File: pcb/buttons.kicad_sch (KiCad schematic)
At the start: 91 parts, among them J3 MSP_SBW, SW1 Off, SW10 R_LCD3, SW11 R_LCD4, SW12 LCD_LEFT, SW13 LCD_RIGHT, SW14 Glow, SW15 Device, SW16 Media, SW17 Mute, SW18 Prev, SW19 Vol+, SW2 Activities, SW20 Vol-, SW21 Ch+, SW22 Ch-, SW23 Dpad_Up, SW24 Dpad_Left, SW25 Dpad_Right, SW26 Dpad_Down, SW27 Dpad_OK, SW28 PgUp, SW29 PgDown, SW3 Help, SW30 Menu, SW31 Exit, SW32 Guide, SW33 Info, SW34 Stop, SW35 Replay, SW36 Skip, SW37 Play, SW38 Rec, SW39 Rew, SW4 L_LCD1, SW40 Fwd, SW41 Pause, SW42 KP_1, SW43 KP_2, SW44 KP_3, SW45 KP_4, SW46 KP_5, SW47 KP_6, SW48 KP_7, SW49 KP_8, SW5 L_LCD2, SW50 KP_9, SW51 KP_0, SW52 KP_Clear, SW53 KP_Enter, SW6 L_LCD3, SW7 L_LCD4, SW8 R_LCD1, SW9 R_LCD2, U1 MSP430G2553IPW28

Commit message: alpha2 pcb
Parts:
- D1, D10, D11, D12, D13, D14, D15, D16, D17, D18, D19, D2, D20, D21, D22, D23, D24, D25, D26, D27, D28, D29, D3, D30, D31, D32, D4, D5, D6, D7, D8, D9: footprint 880+:C265_reverse_mount_led -> 880+:C265_reverse_mount_led_DRC
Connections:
- net +3V3 renamed +3.3V
- net MSP_P1.1 renamed ESP_TO_MSP
- net MSP_P1.2 renamed MSP_TO_ESP

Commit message: current working kikad
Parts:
- added SW54: SW_RollingBall, Resistor_SMD:R_1210_3225Metric, symbol 880+:SW_RollingBall
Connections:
- net GND: now also SW54.1
- net at U1.26 (XOUT/P2.7): now also SW54.2
- no-connect marks 1 -> 0
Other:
- moved on the sheet: C3, C4
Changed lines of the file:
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@@
   (junction (at 76.2 185.42) (diameter 0) (color 0 0 0 0)
   )
+  (junction (at 205.74 128.27) (diameter 0) (color 0 0 0 0)
+  )
   (junction (at 53.34 185.42) (diameter 0) (color 0 0 0 0)
   )
@@
   (junction (at 46.99 33.02) (diameter 0) (color 0 0 0 0)
   )
+  (junction (at 218.44 120.65) (diameter 0) (color 0 0 0 0)
+  )
   (junction (at 99.06 171.45) (diameter 0) (color 0 0 0 0)
   )
@@
   (junction (at 57.15 55.88) (diameter 0) (color 0 0 0 0)
   )
-  (junction (at 228.6 123.19) (diameter 0) (color 0 0 0 0)
-  )
   (junction (at 53.34 132.08) (diameter 0) (color 0 0 0 0)
   )
@@
   (junction (at 57.15 30.48) (diameter 0) (color 0 0 0 0)
   )
+  (junction (at 195.58 119.38) (diameter 0) (color 0 0 0 0)
+  )
   (junction (at 46.99 45.72) (diameter 0) (color 0 0 0 0)
   )
@@
   (junction (at 80.01 71.12) (diameter 0) (color 0 0 0 0)
   )
-  (junction (at 238.76 114.3) (diameter 0) (color 0 0 0 0)
-  )
   (junction (at 68.58 146.05) (diameter 0) (color 0 0 0 0)
   )
@@
   (junction (at 45.72 132.08) (diameter 0) (color 0 0 0 0)
   )
+  (junction (at 218.44 128.27) (diameter 0) (color 0 0 0 0)
+  )
   (junction (at 45.72 146.05) (diameter 0) (color 0 0 0 0)
   )
@@
   (junction (at 80.01 58.42) (diameter 0) (color 0 0 0 0)
   )
+  (junction (at 218.44 111.76) (diameter 0) (color 0 0 0 0)
+  )
   (junction (at 90.17 43.18) (diameter 0) (color 0 0 0 0)
   )
@@
   (junction (at 40.64 55.88) (diameter 0) (color 0 0 0 0)
   )
-  (junction (at 218.44 123.19) (diameter 0) (color 0 0 0 0)
-  )
   (junction (at 83.82 173.99) (diameter 0) (color 0 0 0 0)
   )
@@
   (junction (at 46.99 96.52) (diameter 0) (color 0 0 0 0)
   )
-  (no_connect (at 254 105.41))
   (wire (pts (xy 254 81.28) (xy 256.54 81.28))
     (stroke (width 0) (type default))
@@
     (stroke (width 0) (type default))
   )
+  (wire (pts (xy 218.44 120.65) (xy 241.3 120.65))
+    (stroke (width 0) (type default))
+  )
   (wire (pts (xy 45.72 157.48) (xy 45.72 154.94))
     (stroke (width 0) (type default))
@@
     (stroke (width 0) (type default))
   )
-  (wire (pts (xy 218.44 123.19) (xy 218.44 124.46))
+  (wire (pts (xy 218.44 128.27) (xy 218.44 130.81))
     (stroke (width 0) (type default))
   )
@@
     (stroke (width 0) (type default))
   )
-  (wire (pts (xy 228.6 123.19) (xy 238.76 123.19))
+  (wire (pts (xy 195.58 128.27) (xy 205.74 128.27))
     (stroke (width 0) (type default))
   )
@@
     (stroke (width 0) (type default))
   )
-  (wire (pts (xy 218.44 111.76) (xy 218.44 123.19))
+  (wire (pts (xy 218.44 110.49) (xy 218.44 111.76))
     (stroke (width 0) (type default))
   )
@@
     (stroke (width 0) (type default))
   )
-  (wire (pts (xy 261.62 113.03) (xy 261.62 114.3))
-    (stroke (width 0) (type default))
-  )
   (wire (pts (xy 83.82 146.05) (xy 83.82 147.32))
     (stroke (width 0) (type default))
@@
     (stroke (width 0) (type default))
   )
+  (wire (pts (xy 218.44 120.65) (xy 218.44 128.27))
+    (stroke (width 0) (type default))
+  )
   (wire (pts (xy 53.34 160.02) (xy 53.34 161.29))
     (stroke (width 0) (type default))
@@
     (stroke (width 0) (type default))
   )
+  (wire (pts (xy 254 105.41) (xy 260.35 105.41))
+    (stroke (width 0) (type default))
+  )
   (wire (pts (xy 80.01 45.72) (xy 96.52 45.72))
     (stroke (width 0) (type default))
@@
     (stroke (width 0) (type default))
   )
-  (wire (pts (xy 218.44 123.19) (xy 228.6 123.19))
+  (wire (pts (xy 205.74 128.27) (xy 218.44 128.27))
     (stroke (width 0) (type default))
   )
@@
     (stroke (width 0) (type default))
   )
-  (wire (pts (xy 228.6 123.19) (xy 228.6 121.92))
+  (wire (pts (xy 195.58 128.27) (xy 195.58 127))
     (stroke (width 0) (type default))
   )
@@
     (stroke (width 0) (type default))
   )
-  (wire (pts (xy 238.76 123.19) (xy 238.76 121.92))
+  (wire (pts (xy 205.74 128.27) (xy 205.74 127))
     (stroke (width 0) (type default))
   )
@@
     (stroke (width 0) (type default))
   )
+  (wire (pts (xy 260.35 105.41) (xy 260.35 120.65))
+    (stroke (width 0) (type default))
+  )
   (wire (pts (xy 90.17 68.58) (xy 90.17 55.88))
     (stroke (width 0) (type default))
@@
     (stroke (width 0) (type default))
   )
+  (wire (pts (xy 260.35 120.65) (xy 251.46 120.65))
+    (stroke (width 0) (type default))
+  )
   (wire (pts (xy 60.96 157.48) (xy 68.58 157.48))
     (stroke (width 0) (type default))
@@
     (stroke (width 0) (type default))
   )
-  (wire (pts (xy 261.62 114.3) (xy 238.76 114.3))
-    (stroke (width 0) (type default))
-  )
   (wire (pts (xy 63.5 96.52) (xy 80.01 96.52))
     (stroke (width 0) (type default))
@@
     (stroke (width 0) (type default))
   )
-  (wire (pts (xy 228.6 114.3) (xy 238.76 114.3))
+  (wire (pts (xy 195.58 119.38) (xy 205.74 119.38))
+    (stroke (width 0) (type default))
+  )
+  (wire (pts (xy 218.44 111.76) (xy 218.44 120.65))
     (stroke (width 0) (type default))
   )
@@
     )
   )
-  (symbol (lib_id "power:GND") (at 218.44 124.46 0) (unit 1)
+  (symbol (lib_id "power:GND") (at 218.44 130.81 0) (unit 1)
     (in_bom yes) (on_board yes) (dnp no) (fields_autoplaced)
-    (property "Reference" "#PWR06" (at 218.44 130.81 0)
+    (property "Reference" "#PWR06" (at 218.44 137.16 0)
       (effects (font (size 1.27 1.27)) hide)
     )
-    (property "Value" "GND" (at 218.44 129.0225 0)
+    (property "Value" "GND" (at 218.44 135.3725 0)
       (effects (font (size 1.27 1.27)))
     )
-    (property "Footprint" "" (at 218.44 124.46 0)
+    (property "Footprint" "" (at 218.44 130.81 0)
       (effects (font (size 1.27 1.27)) hide)
     )
-    (property "Datasheet" "" (at 218.44 124.46 0)
+    (property "Datasheet" "" (at 218.44 130.81 0)
       (effects (font (size 1.27 1.27)) hide)
     )
@@
     )
   )
+  (symbol (lib_id "880+:SW_RollingBall") (at 246.38 120.65 0) (unit 1)
+    (in_bom yes) (on_board yes) (dnp no) (fields_autoplaced)
+    (property "Reference" "SW54" (at 246.38 115.57 0)
+      (effects (font (size 1.27 1.27)))
+    )
+    (property "Value" "SW_RollingBall" (at 246.38 118.11 0)
+      (effects (font (size 1.27 1.27)))
+    )
+    (property "Footprint" "Resistor_SMD:R_1210_3225Metric" (at 246.38 120.65 0)
+      (effects (font (size 1.27 1.27)) hide)
+    )
+    (property "Datasheet" "~" (at 246.38 120.65 0)
+      (effects (font (size 1.27 1.27)) hide)
+    )
+    (pin "1")
+    (pin "2")
+    (instances
+      (project "800+"
+        (path "/e63e39d7-6ac0-4ffd-8aa3-1841a4541b55/ceed2ac1-ff2d-4a48-84e5-5f8d5045fc04"
+          (reference "SW54") (unit 1)
+        )
+      )
+    )
+  )
   (symbol (lib_id "Device:LED") (at 45.72 179.07 90) (unit 1)
     (in_bom yes) (on_board yes) (dnp no) (fields_autoplaced)
@@
     )
   )
-  (symbol (lib_id "power:+3.3V") (at 261.62 113.03 0) (unit 1)
+  (symbol (lib_id "power:+3.3V") (at 195.58 119.38 0) (unit 1)
     (in_bom yes) (on_board yes) (dnp no)
-    (property "Reference" "#PWR019" (at 261.62 116.84 0)
+    (property "Reference" "#PWR019" (at 195.58 123.19 0)
       (effects (font (size 1.27 1.27)) hide)
     )
-    (property "Value" "+3.3V" (at 261.62 109.22 0)
+    (property "Value" "+3.3V" (at 195.58 115.57 0)
       (effects (font (size 1.27 1.27)))
     )
-    (property "Footprint" "" (at 261.62 113.03 0)
+    (property "Footprint" "" (at 195.58 119.38 0)
       (effects (font (size 1.27 1.27)) hide)
     )
-    (property "Datasheet" "" (at 261.62 113.03 0)
+    (property "Datasheet" "" (at 195.58 119.38 0)
       (effects (font (size 1.27 1.27)) hide)
     )
@@
     )
   )
-  (symbol (lib_id "Device:C") (at 228.6 118.11 0) (unit 1)
+  (symbol (lib_id "Device:C") (at 195.58 123.19 0) (unit 1)
     (in_bom yes) (on_board yes) (dnp no) (fields_autoplaced)
-    (property "Reference" "C3" (at 231.521 117.2015 0)
+    (property "Reference" "C3" (at 198.501 122.2815 0)
       (effects (font (size 1.27 1.27)) (justify left))
     )
-    (property "Value" "10u" (at 231.521 119.9766 0)
+    (property "Value" "10u" (at 198.501 125.0566 0)
       (effects (font (size 1.27 1.27)) (justify left))
     )
-    (property "Footprint" "Capacitor_SMD:C_0805_2012Metric" (at 229.5652 121.92 0)
+    (property "Footprint" "Capacitor_SMD:C_0805_2012Metric" (at 196.5452 127 0)
       (effects (font (size 1.27 1.27)) hide)
     )
-    (property "Datasheet" "~" (at 228.6 118.11 0)
+    (property "Datasheet" "~" (at 195.58 123.19 0)
       (effects (font (size 1.27 1.27)) hide)
     )
@@
     )
   )
-  (symbol (lib_id "Device:C") (at 238.76 118.11 0) (unit 1)
+  (symbol (lib_id "Device:C") (at 205.74 123.19 0) (unit 1)
     (in_bom yes) (on_board yes) (dnp no) (fields_autoplaced)
-    (property "Reference" "C4" (at 241.681 117.2015 0)
+    (property "Reference" "C4" (at 208.661 122.2815 0)
       (effects (font (size 1.27 1.27)) (justify left))
     )
-    (property "Value" ".1u" (at 241.681 119.9766 0)
+    (property "Value" ".1u" (at 208.661 125.0566 0)
       (effects (font (size 1.27 1.27)) (justify left))
     )
-    (property "Footprint" "Capacitor_SMD:C_0805_2012Metric" (at 239.7252 121.92 0)
+    (property "Footprint" "Capacitor_SMD:C_0805_2012Metric" (at 206.7052 127 0)
       (effects (font (size 1.27 1.27)) hide)
     )
-    (property "Datasheet" "~" (at 238.76 118.11 0)
+    (property "Datasheet" "~" (at 205.74 123.19 0)
       (effects (font (size 1.27 1.27)) hide)
     )

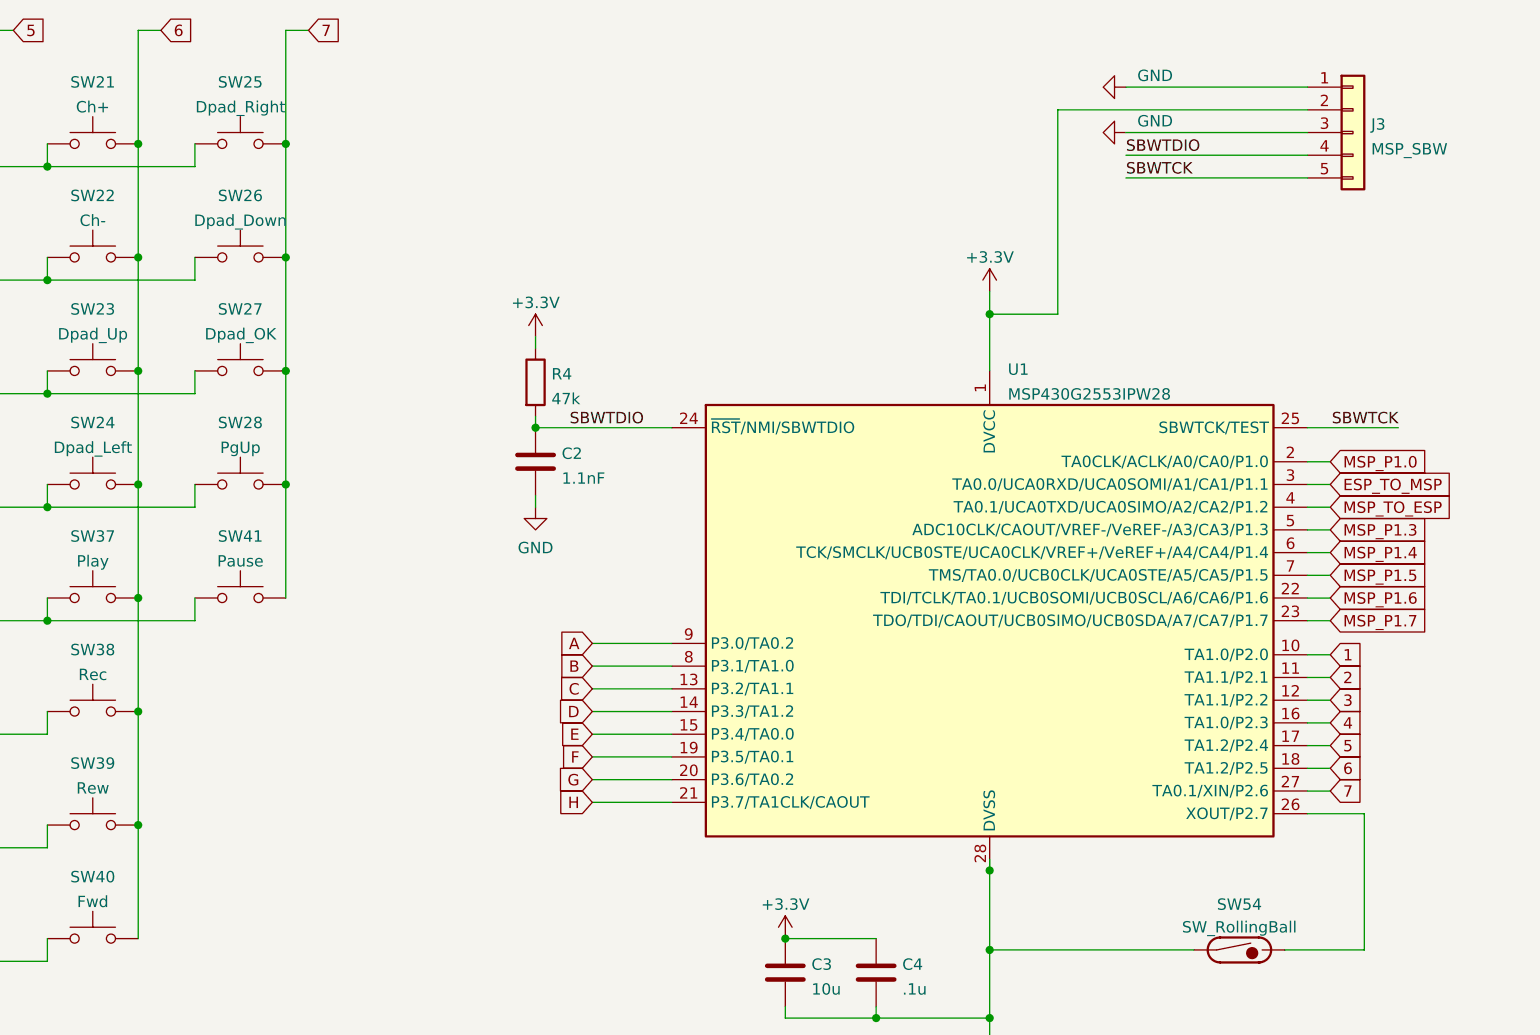
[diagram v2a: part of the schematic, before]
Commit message: add power to schematic
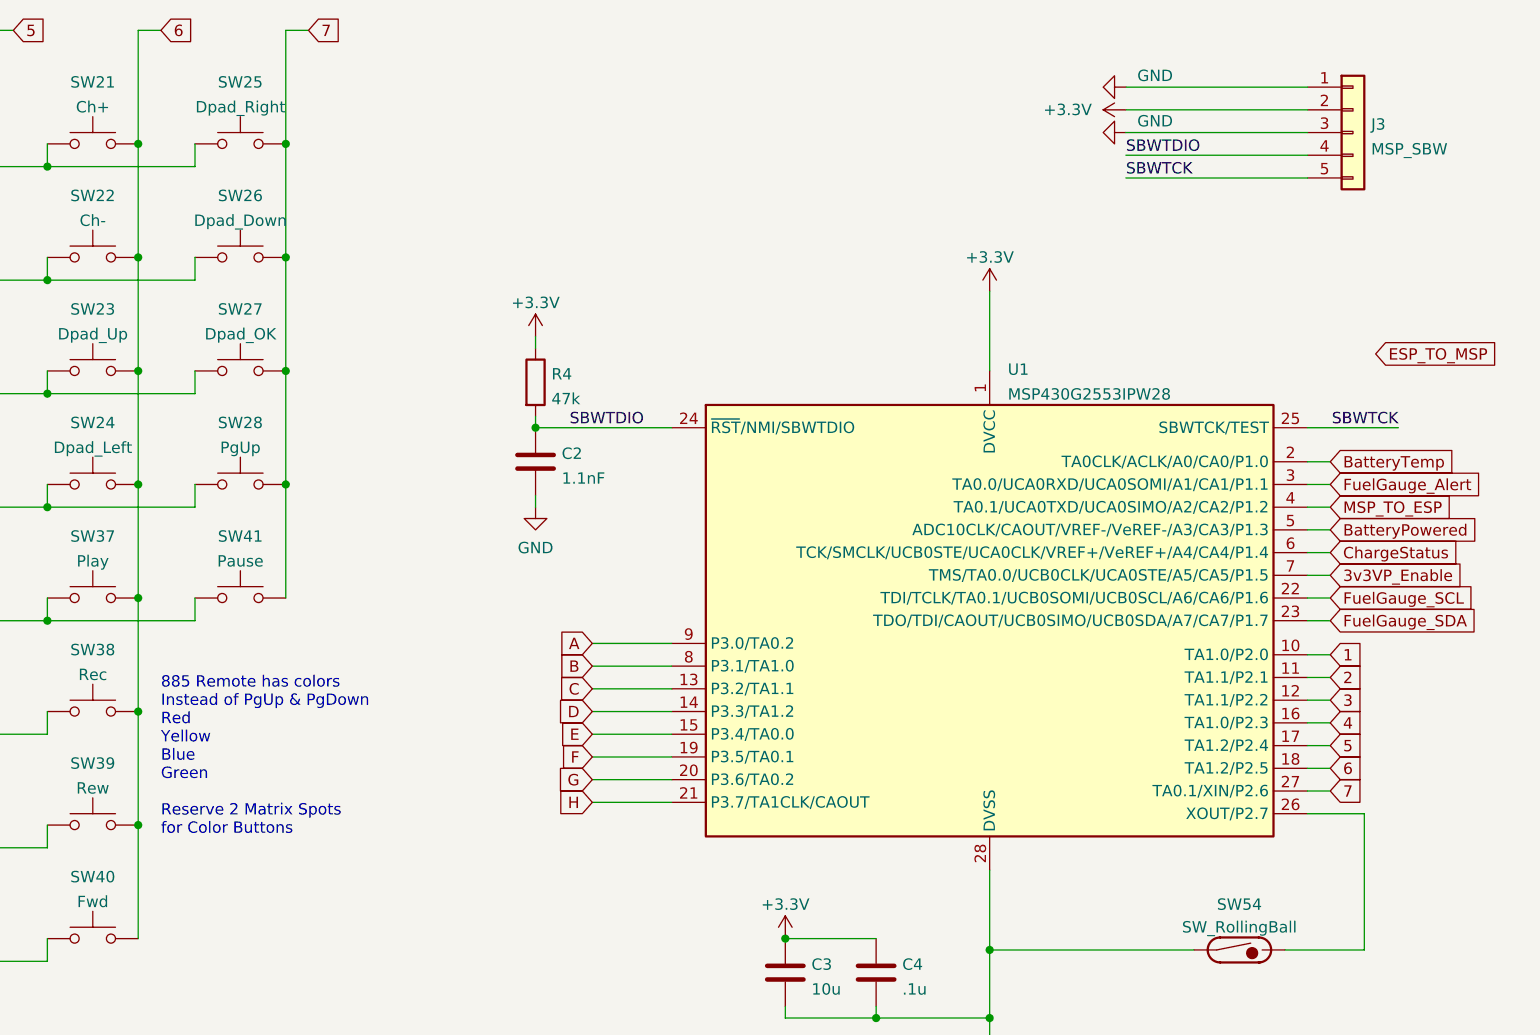
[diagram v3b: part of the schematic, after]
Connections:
- net ESP_TO_MSP: no longer U1.3 (TA0.0/UCA0RXD/UCA0SOMI/A1/CA1/P1.1)
- net MSP_P1.0 renamed BatteryTemp
- net MSP_P1.3 renamed BatteryPowered
- net MSP_P1.4 renamed ChargeStatus
- net MSP_P1.5 renamed 3v3VP_Enable
- net MSP_P1.6 renamed FuelGauge_SCL
- net MSP_P1.7 renamed FuelGauge_SDA
- new net FuelGauge_Alert: U1.3 (TA0.0/UCA0RXD/UCA0SOMI/A1/CA1/P1.1)
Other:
- note added: "885 Remote has colors Instead of PgUp & PgDown Red Yellow Blue Green Reserve 2 Matrix Spots for Color Buttons"

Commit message: more schematic updates
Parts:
- added R16, R17: 4.7k, Resistor_SMD:R_0805_2012Metric, symbol Device:R
- added SW54, SW55: Pause, 880+:4mm Dome, symbol Switch:SW_Push
- SW28: value PgUp -> PgUp/Grn
- SW29: value PgDown -> PgDown/Yel
- renumbered SW54 to SW56
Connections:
- net +3.3V: now also R16.1, R17.2
- net 7: now also SW54.2, SW55.2
- net F: now also SW54.1
- net FuelGauge_SCL: now also R16.2
- net FuelGauge_SDA: now also R17.1
- net G: now also SW55.1
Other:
- note added: "885 895 Remotes have colors Instead of PgUp & PgDown"
- note removed: "885 Remote has colors Instead of PgUp & PgDown Red Yellow Blue Green Reserve 2 Matrix Spots for Color Buttons"

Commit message: ready to route????
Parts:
- SW54: value Pause -> Red
- SW55: value Pause -> Blue
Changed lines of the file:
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@@
       (effects (font (size 1.27 1.27)))
     )
-    (property "Value" "Pause" (at 134.62 101.6 0)
+    (property "Value" "Blue" (at 134.62 101.6 0)
       (effects (font (size 1.27 1.27)))
     )
@@
       (effects (font (size 1.27 1.27)))
     )
-    (property "Value" "Pause" (at 134.62 88.9 0)
-      (effects (font (size 1.27 1.27)))
-    )
+    (property "Value" "Red" (at 134.62 88.9 0)
+      (effects (font (size 1.27 1.27)))
+    )

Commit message: parts placed
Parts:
- added D10, D11, D20, D21, D22, D31, D32, D33, D36, D37, D44, D9: LED, 880+:C265_reverse_mount_led_DRC, symbol Device:LED
- renumbered D9 to D12, D10 to D13, D11 to D14, D12 to D15, D13 to D16, D14 to D17, D15 to D18, D16 to D19, D17 to D23, D18 to D24, D19 to D25, D20 to D26, D21 to D27, D22 to D28, D23 to D29, D24 to D30, D25 to D34, D26 to D35, D27 to D38, D28 to D39, D29 to D40, D30 to D41, D31 to D42, D32 to D43
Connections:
- net GND: now also D10.1 (K), D11.1 (K), D20.1 (K), D21.1 (K), D22.1 (K), D31.1 (K), D32.1 (K), D33.1 (K), D36.1 (K), D37.1 (K), D44.1 (K), D9.1 (K)
- net LED_PWM: now also D10.2 (A), D11.2 (A), D20.2 (A), D21.2 (A), D22.2 (A), D31.2 (A), D32.2 (A), D33.2 (A), D36.2 (A), D37.2 (A), D44.2 (A), D9.2 (A)
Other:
- moved on the sheet: D38, D39, D40, D41, D42, D43

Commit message: alpha3 pcb
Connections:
- net ChargeStatus: now also U1.3 (TA0.0/UCA0RXD/UCA0SOMI/A1/CA1/P1.1); no longer U1.6 (TCK/SMCLK/UCB0STE/UCA0CLK/VREF+/VeREF+/A4/CA4/P1.4)
- net FuelGauge_Alert: now also U1.6 (TCK/SMCLK/UCB0STE/UCA0CLK/VREF+/VeREF+/A4/CA4/P1.4); no longer U1.3 (TA0.0/UCA0RXD/UCA0SOMI/A1/CA1/P1.1)
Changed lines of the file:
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@@
-    )
-  )
-  (global_label "ESP_TO_MSP" (shape input) (at 261.62 53.975 0) (fields_autoplaced)
-    (effects (font (size 1.27 1.27)) (justify left))
-    (property "Intersheetrefs" "${INTERSHEET_REFS}" (at 276.3185 53.975 0)
-      (effects (font (size 1.27 1.27)) (justify left) hide)
     )
   )
@@
     )
   )
-  (global_label "ChargeStatus" (shape input) (at 256.54 76.2 0) (fields_autoplaced)
+  (global_label "ChargeStatus" (shape input) (at 256.54 68.58 0) (fields_autoplaced)
     (effects (font (size 1.27 1.27)) (justify left))
-    (property "Intersheetrefs" "${INTERSHEET_REFS}" (at 272.104 76.2 0)
+    (property "Intersheetrefs" "${INTERSHEET_REFS}" (at 272.104 68.58 0)
       (effects (font (size 1.27 1.27)) (justify left) hide)
     )
@@
     )
   )
-  (global_label "FuelGauge_Alert" (shape input) (at 256.54 68.58 0) (fields_autoplaced)
+  (global_label "FuelGauge_Alert" (shape input) (at 256.54 76.2 0) (fields_autoplaced)
     (effects (font (size 1.27 1.27)) (justify left))
-    (property "Intersheetrefs" "${INTERSHEET_REFS}" (at 274.6441 68.58 0)
+    (property "Intersheetrefs" "${INTERSHEET_REFS}" (at 274.6441 76.2 0)
       (effects (font (size 1.27 1.27)) (justify left) hide)
     )
